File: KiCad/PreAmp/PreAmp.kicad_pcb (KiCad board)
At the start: 2 copper layers, 95.2 x 82.6 mm, 149 parts, among them J1 CONN_01X02, J2 CONN_01X02, J3 CONN_01X02, J4 CONN_01X02, J5 CONN_01X02, J6 CONN_01X02, K1 G6K-2F, K2 G6K-2F, K3 G6K-2F, K4 G6K-2F, K5 G6K-2F, P1 A-POWER, P13 CTRL_VOLUME, P14 RSA-IN2L, P15 RSA-IN2R, P16 RSA-IN3L, P17 RSA-IN3R, P2 RSA-IN1L, P3 RSA-INTL, P4 RSA-IN1R, P5 RSA-INTR, P8 CTRL_RELAYS, Q1 BC817, Q2 BC817, Q3 BC817, Q4 BC817, Q5 BC817, U1 78M15, U2 79M15, U3 78L05, U4 78L05, U5 79L05, U6 NE5532, U7 NE5532, U8 PGA4311, U9 TL074

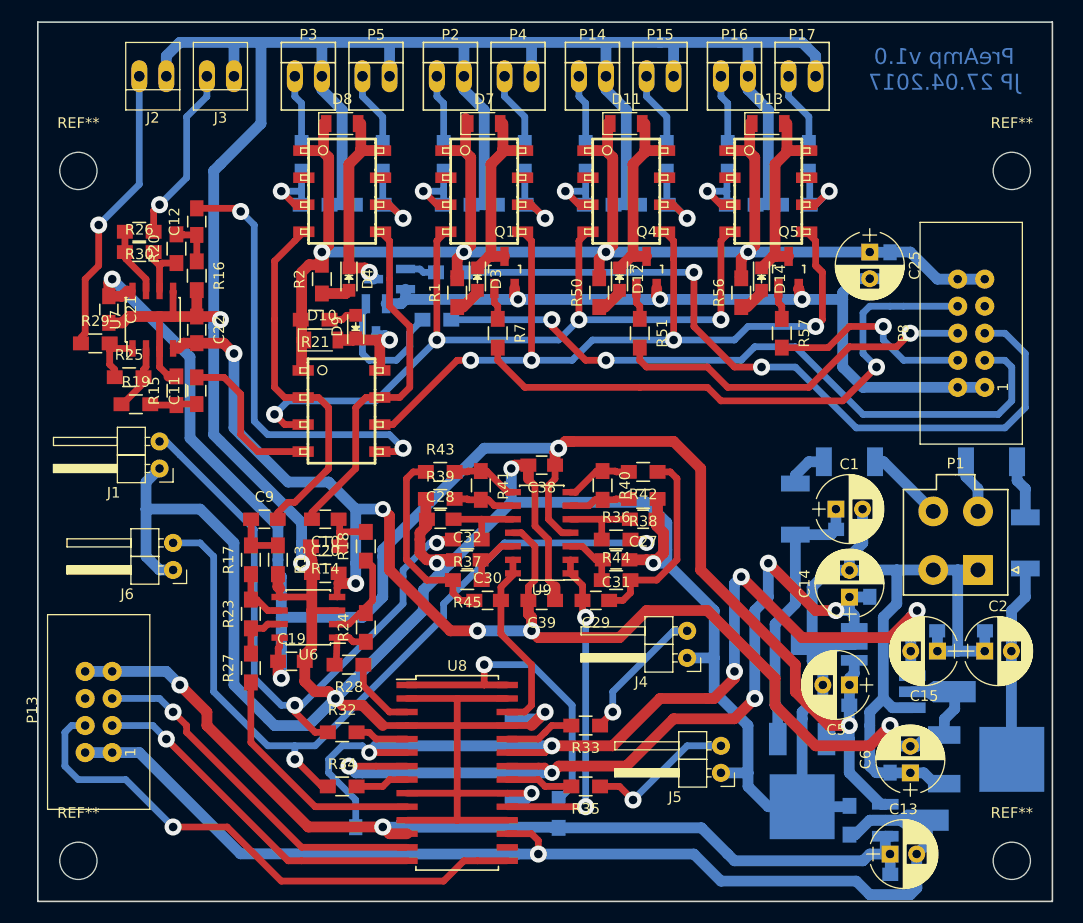
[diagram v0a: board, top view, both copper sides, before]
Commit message: PreAmp PCP pimped
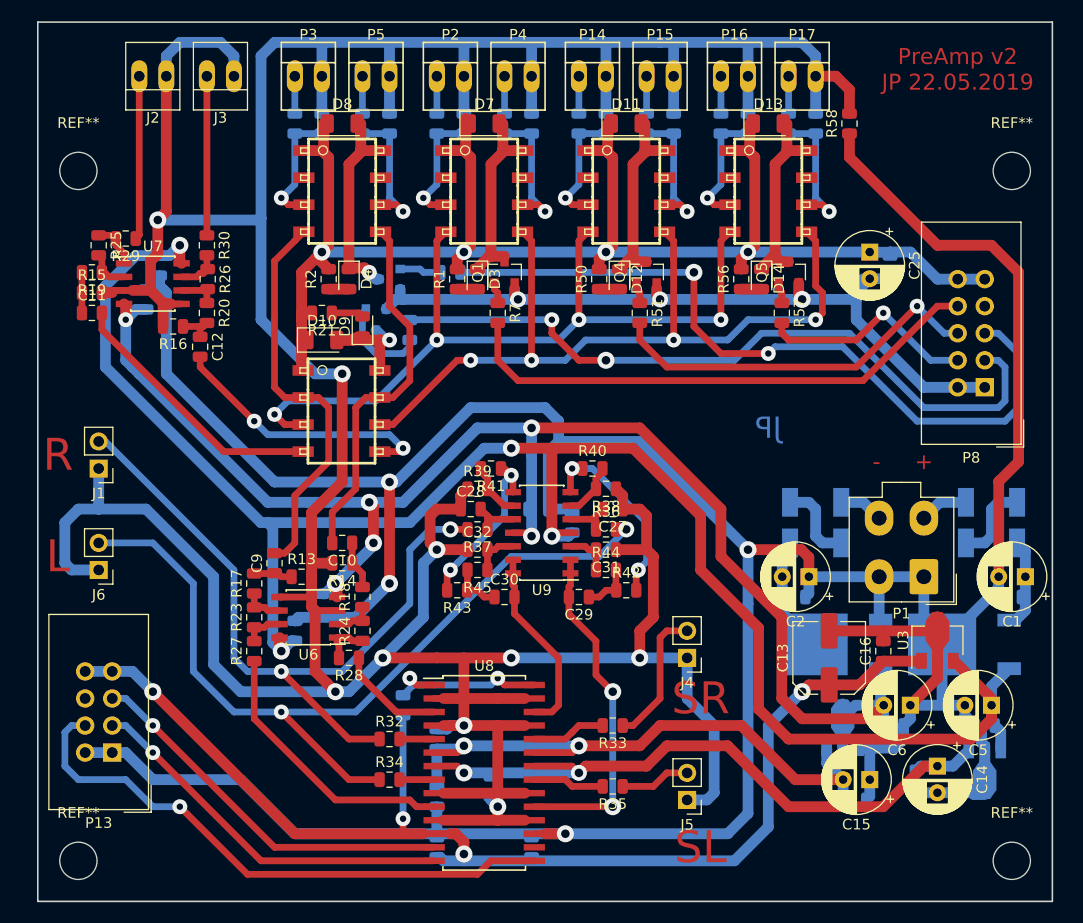
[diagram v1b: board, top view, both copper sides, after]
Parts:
- C1, C14, C15, C2, C25, C5, C6: footprint Capacitors_THT:CP_Radial_D6.3mm_P2.50mm -> Capacitor_THT:CP_Radial_D6.3mm_P2.50mm
- C10, C11, C12, C17, C18, C26, C27, C28, C29, C3, C30, C31, C32, C33, C34, C35, C36, C37, C4, C7, C8, C9: footprint Capacitors_SMD:C_0805_HandSoldering -> Capacitor_SMD:C_0805_2012Metric
- C13: footprint Capacitors_THT:CP_Radial_D6.3mm_P2.50mm -> Capacitor_SMD:C_Elec_6.3x5.8
- C16: footprint Capacitors_SMD:C_0805_HandSoldering -> Capacitor_SMD:C_0805_2012Metric; moved to F.Cu
- C19, C20, C21, C22, C38, C39: footprint Capacitors_SMD:C_0805_HandSoldering -> Capacitor_SMD:C_0805_2012Metric; moved to B.Cu
- D1, D2, D5, D6: footprint Diodes_SMD:D_MELF_Standard -> Diode_SMD:D_MELF
- D10, D11, D13, D7, D8: footprint Diodes_SMD:D_1206 -> Diode_SMD:D_1206_3216Metric
- D12, D14, D3, D4, D9: footprint LEDs:LED_0805 -> LED_SMD:LED_0805_2012Metric
- J1, J4, J5, J6: footprint Pin_Headers:Pin_Header_Angled_1x02_Pitch2.54mm -> Connector_PinHeader_2.54mm:PinHeader_1x02_P2.54mm_Vertical
- P1: footprint Connectors_Molex:Molex_MiniFit-JR-5556-04A_2x02x4.20mm_Straight -> Connector_Molex:Molex_Mini-Fit_Jr_5566-04A_2x02_P4.20mm_Vertical
- P13: footprint Connectors:IDC_Header_Straight_8pins -> Connector_IDC:IDC-Header_2x04_P2.54mm_Vertical
- P8: footprint Connectors:IDC_Header_Straight_10pins -> Connector_IDC:IDC-Header_2x05_P2.54mm_Vertical
- Q1, Q2, Q3, Q4, Q5: footprint TO_SOT_Packages_SMD:SOT-23_Handsoldering -> Package_TO_SOT_SMD:SOT-23
- R1, R10, R11, R12, R13, R14, R15, R16, R17, R18, R19, R2, R20, R21, R22, R23, R24, R25, R26, R27, R28, R29, R3, R30, R31, R32, R33, R34, R35, R36, R37, R38, R39, R4, R40, R41, R42, R43, R44, R45, R46, R47, R48, R49, R5, R50, R51, R52, R53, R54, R55, R56, R57, R6, R7, R8, R9: footprint Resistors_SMD:R_0805_HandSoldering -> Resistor_SMD:R_0805_2012Metric
- R58: footprint Resistors_SMD:R_0805_HandSoldering -> Resistor_SMD:R_0805_2012Metric; moved to F.Cu
- U1, U2: footprint TO_SOT_Packages_SMD:TO-252-2Lead -> Package_TO_SOT_SMD:TO-252-2
- U3: footprint TO_SOT_Packages_SMD:SOT89-3_Housing_Handsoldering -> Package_TO_SOT_SMD:SOT-89-3; moved to F.Cu
- U4, U5: footprint TO_SOT_Packages_SMD:SOT89-3_Housing_Handsoldering -> Package_TO_SOT_SMD:SOT-89-3
- U6, U7: footprint Housings_SOIC:SOIC-8_3.9x4.9mm_Pitch1.27mm -> Package_SO:SOIC-8_3.9x4.9mm_P1.27mm
- U8: footprint Housings_SOIC:SOIC-28_7.5x17.9mm_Pitch1.27mm -> Package_SO:SOIC-28W_7.5x17.9mm_P1.27mm
- U9: footprint Housings_SOIC:SOIC-14_3.9x8.7mm_Pitch1.27mm -> Package_SO:SOIC-14_3.9x8.7mm_P1.27mm
- moved R58 65.4 mm to (101.6, 34.9)
- moved C16 21.0 mm to (104.8, 84.5), turned to 90 degrees
- moved D6 19.7 mm to (98.4, 74.3), turned to 180 degrees
- moved C4 19.3 mm to (96.5, 79.4), turned to 180 degrees
- moved C13 19.3 mm to (99.7, 85.1), turned to 90 degrees
- moved C17 18.9 mm to (108.0, 96.5), turned to 270 degrees
- moved C1 18.9 mm to (118.1, 77.5), turned to 180 degrees
- moved D5 18.7 mm to (114.9, 74.3), turned to 180 degrees
- moved U4 18.5 mm to (114.3, 95.2)
- moved C2 17.9 mm to (97.8, 77.5), turned to 180 degrees
- moved C14 17.9 mm to (109.9, 95.2), turned to 270 degrees
- moved R31 17.8 mm to (59.7, 89.5)
- moved U1 17.6 mm to (112.4, 83.8), turned to 180 degrees
- moved C18 17.1 mm to (102.2, 98.4)
- moved D2 16.9 mm to (98.4, 70.5), turned to 180 degrees
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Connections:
- net /IN-B-L renamed InBuffL
- net /IN-B-R renamed InBuffR
- C1 pad 2: GNDA -> GNDPWR
- C13 pad 2: GNDD -> GNDPWR
- C14 pad 2: GNDA -> GNDPWR
- C15 pad 1: GNDA -> GNDPWR
- C16 pad 2: GNDD -> GNDPWR
- C17 pad 2: GNDA -> GNDPWR
- C18 pad 1: GNDA -> GNDPWR
- C19 pad 2: GNDA -> GNDPWR
- C2 pad 1: GNDA -> GNDPWR
- C20 pad 1: GNDA -> GNDPWR
- C21 pad 2: GNDA -> GNDPWR
- C22 pad 1: GNDA -> GNDPWR
- C3 pad 2: GNDA -> GNDPWR
- C35 pad 2: GNDD -> GNDPWR
- C36 pad 2: GNDD -> GNDPWR
- C37 pad 2: GNDD -> GNDPWR
- C38 pad 2: GNDA -> GNDPWR
- C39 pad 1: GNDA -> GNDPWR
- C4 pad 1: GNDA -> GNDPWR
- C5 pad 2: GNDA -> GNDPWR
- C6 pad 1: GNDA -> GNDPWR
- C7 pad 2: GNDA -> GNDPWR
- C8 pad 1: GNDA -> GNDPWR
- P1 pad 1: GNDA -> GNDPWR
- P1 pad 2: GNDA -> GNDPWR
- P1 pad 3: Net-(D2-Pad1) -> Net-(D1-Pad2)
- P1 pad 4: Net-(D1-Pad2) -> Net-(D2-Pad1)
- P13 pad 1: GNDD -> GNDPWR
- P13 pad 2: GNDD -> GNDPWR
- R58 pad 1: GNDD -> GNDPWR
- U1 pad 2: GNDA -> GNDPWR
- U2 pad 1: GNDA -> GNDPWR
- U3 pad 2: GNDD -> GNDPWR
- U4 pad 2: GNDA -> GNDPWR
- U5 pad 1: GNDA -> GNDPWR
- U8 pad 17: GNDD -> GNDPWR
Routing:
- net GNDPWR: track 0.00 -> 360.3 mm, vias 0 -> 4
- net GNDA: track 600.2 -> 432.3 mm, vias 8 -> 9
- net GNDD: track 103.2 -> 0.00 mm, vias 1 -> 0
- net -5V: track 93.4 -> 57.8 mm, vias 5 -> 2
- net +5VD: track 92.2 -> 114.7 mm, vias 2 -> 4
- net Net-(C1-Pad1): track 26.4 -> 8.56 mm
- net +5V: track 78.9 -> 62.6 mm, vias 5 -> 2
- net /OUT-T-R: track 41.8 -> 25.5 mm
- net Net-(R31-Pad1): track 30.5 -> 16.6 mm, vias 1 -> 2
- net Net-(C29-Pad1): track 18.6 -> 4.75 mm
- net Net-(C30-Pad1): track 18.6 -> 5.08 mm
- net Net-(R40-Pad1): track 7.24 -> 19.1 mm, vias 0 -> 2
- net /OUT-TB-L: track 26.8 -> 15.4 mm, vias 1 -> 0
- net -15V: track 133.1 -> 144.3 mm
- net /OUT-T-L: track 15.1 -> 25.2 mm
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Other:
- net class Default: via_dia 1.6 -> 1.4; via_drill 0.8 -> 0.6
- board text added: "+"
- board text added: "-"
- board text added: "JP"
- board text added: "L"
- board text added: "PreAmp v2 JP 22.05.2019"
- board text added: "R"
- board text added: "SL"
- board text added: "SR"
- board text removed: "PreAmp v1.0 JP 27.04.2017"

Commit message: Last tweaks
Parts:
- added REF**: PinHeader_1x01_P1.27mm_Vertical, Connector_PinHeader_1.27mm:PinHeader_1x01_P1.27mm_Vertical, F.Cu at (106.7, 34.9)
- moved J1 1.91 mm to (31.1, 65.4)
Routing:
- net GNDA: track 432.3 -> 439.4 mm
- net OUT-R: track 68.8 -> 71.0 mm
- net GNDPWR: track 360.3 -> 359.6 mm
- net +5VD: track 114.7 -> 114.0 mm

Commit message: Silk stuff
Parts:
- moved J2 2.54 mm to (34.9, 30.5), turned to 0 degrees
- moved J3 2.54 mm to (41.3, 30.5), turned to 0 degrees
- renumbered REF** to GNDA
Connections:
- J2 pad 1: GNDA -> /OUT-TB-L
- J2 pad 2: /OUT-TB-L -> GNDA
- J3 pad 1: GNDA -> /OUT-TB-R
- J3 pad 2: /OUT-TB-R -> GNDA
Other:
- board text added: "IN1"
- board text added: "IN2"
- board text added: "IN3"
- board text added: "PreAmp v2 JP 24.05.2019"
- board text added: "TL-I"
- board text added: "TL-O"
- board text removed: "PreAmp v2 JP 22.05.2019"
